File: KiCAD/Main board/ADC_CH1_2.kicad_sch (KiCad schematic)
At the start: 31 parts, among them U27 PCM1804, U5 OPA1632DR, U6 LM4562

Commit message: Worked on main board SCH
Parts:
- removed C21, C25, C26: 100nF, symbol Device:C
- removed C22, C28, C30, C4: 22uF, symbol Device:C_Polarized
- removed C35: 100n, symbol Device:C
- removed R31, R32, R36, R38: 10, symbol Device:R
- added C1 (x4): 100n, Capacitor_SMD:C_0402_1005Metric, symbol Device:C
- added C3 (x4): 22uF, Capacitor_THT:CP_Radial_D5.0mm_P2.00mm, symbol Device:C_Polarized
- added R1 (x4): 10R, Resistor_SMD:R_0805_2012Metric, symbol Device:R
- R13: value 2.7k -> 2k7
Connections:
- net +12V: now also R1.1, R1.1
- net -12V: now also R1.2, R1.2
- net GND: now also C1.1, C1.1, C1.2, C1.2, C3.1, C3.1, C3.2, C3.2
- net at U6.8 (V+): now also C1.1, C3.1, R1.2
- net at U5.3 (V+): now also C1.1, C3.1, R1.2
- net at U6.4 (V-): now also C1.2, C3.2, R1.1
- net at U5.6 (V-): now also C1.2, C3.2, R1.1
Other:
- moved on the sheet: C40, R45, U6B, U6C

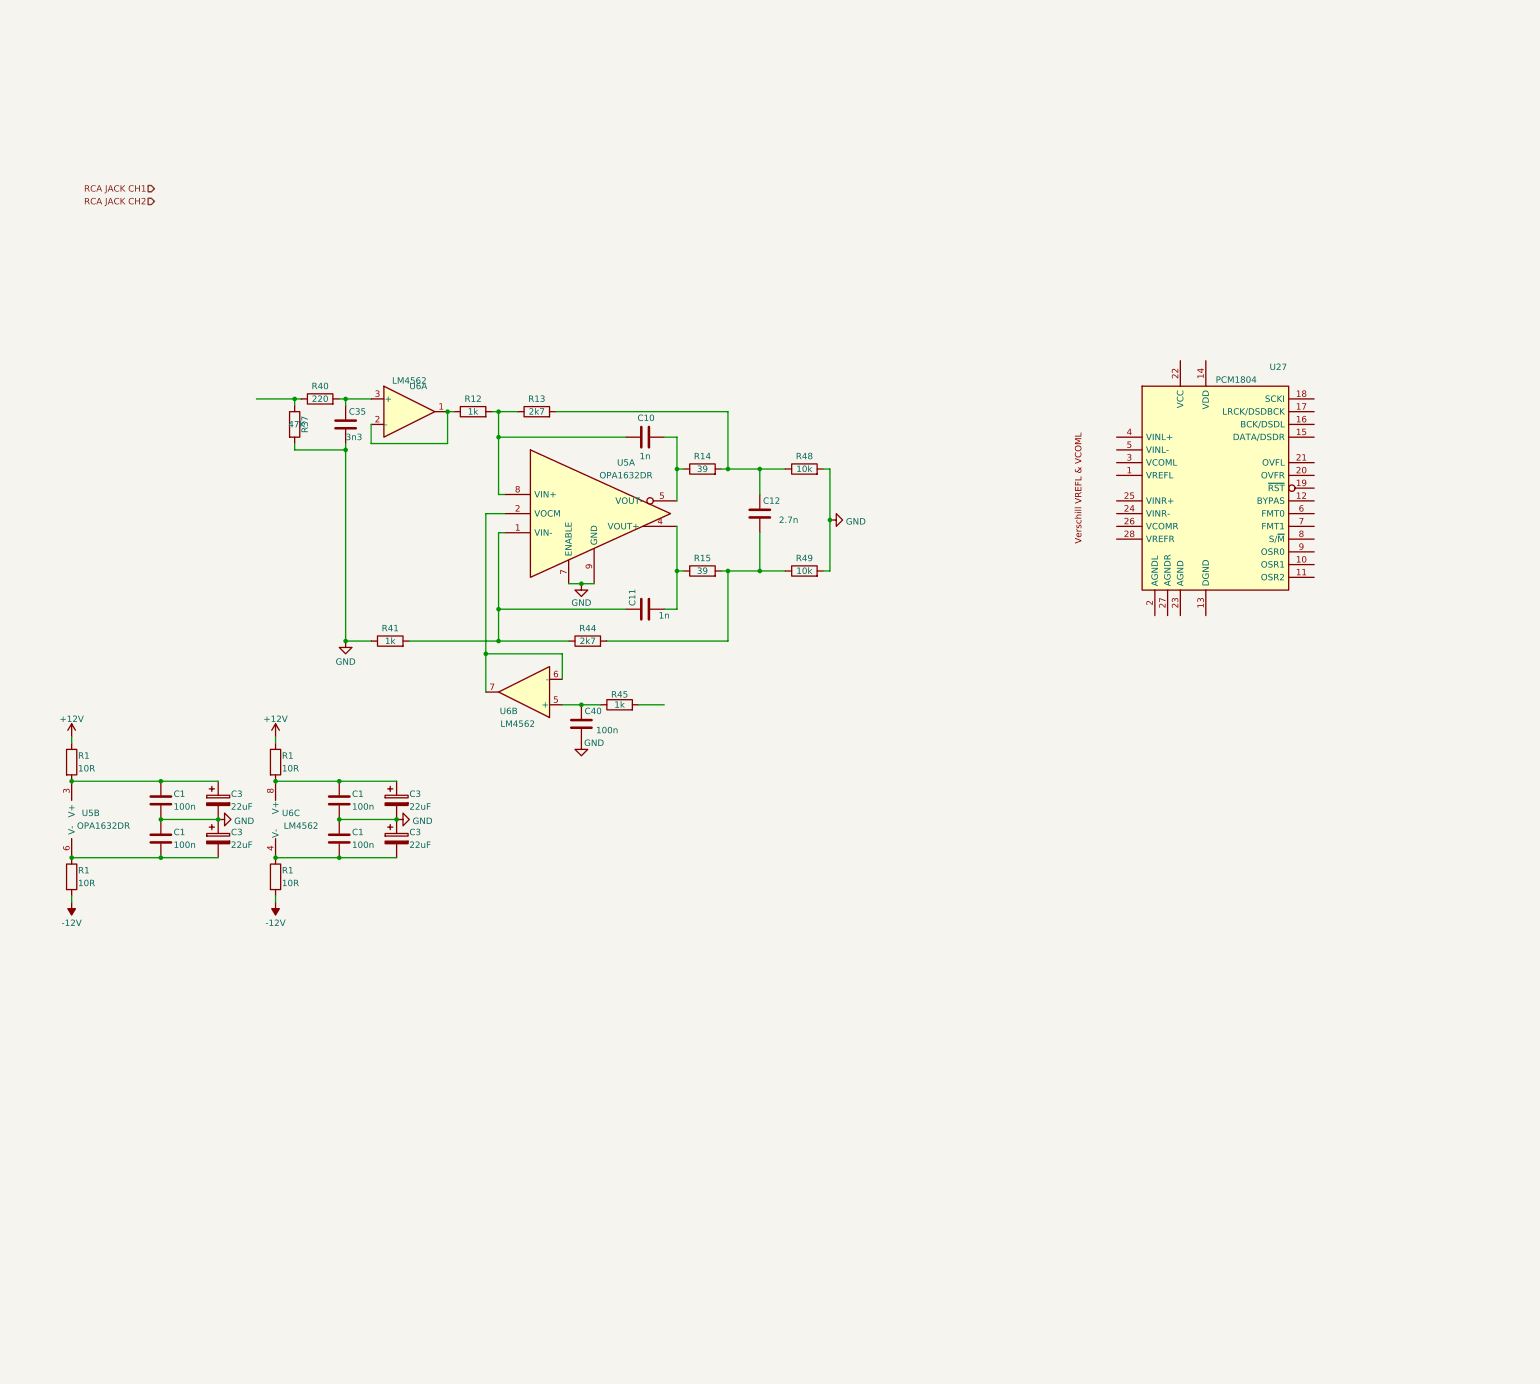
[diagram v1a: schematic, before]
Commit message: Worked on main board schematic and PCB, added symbols to symbol library
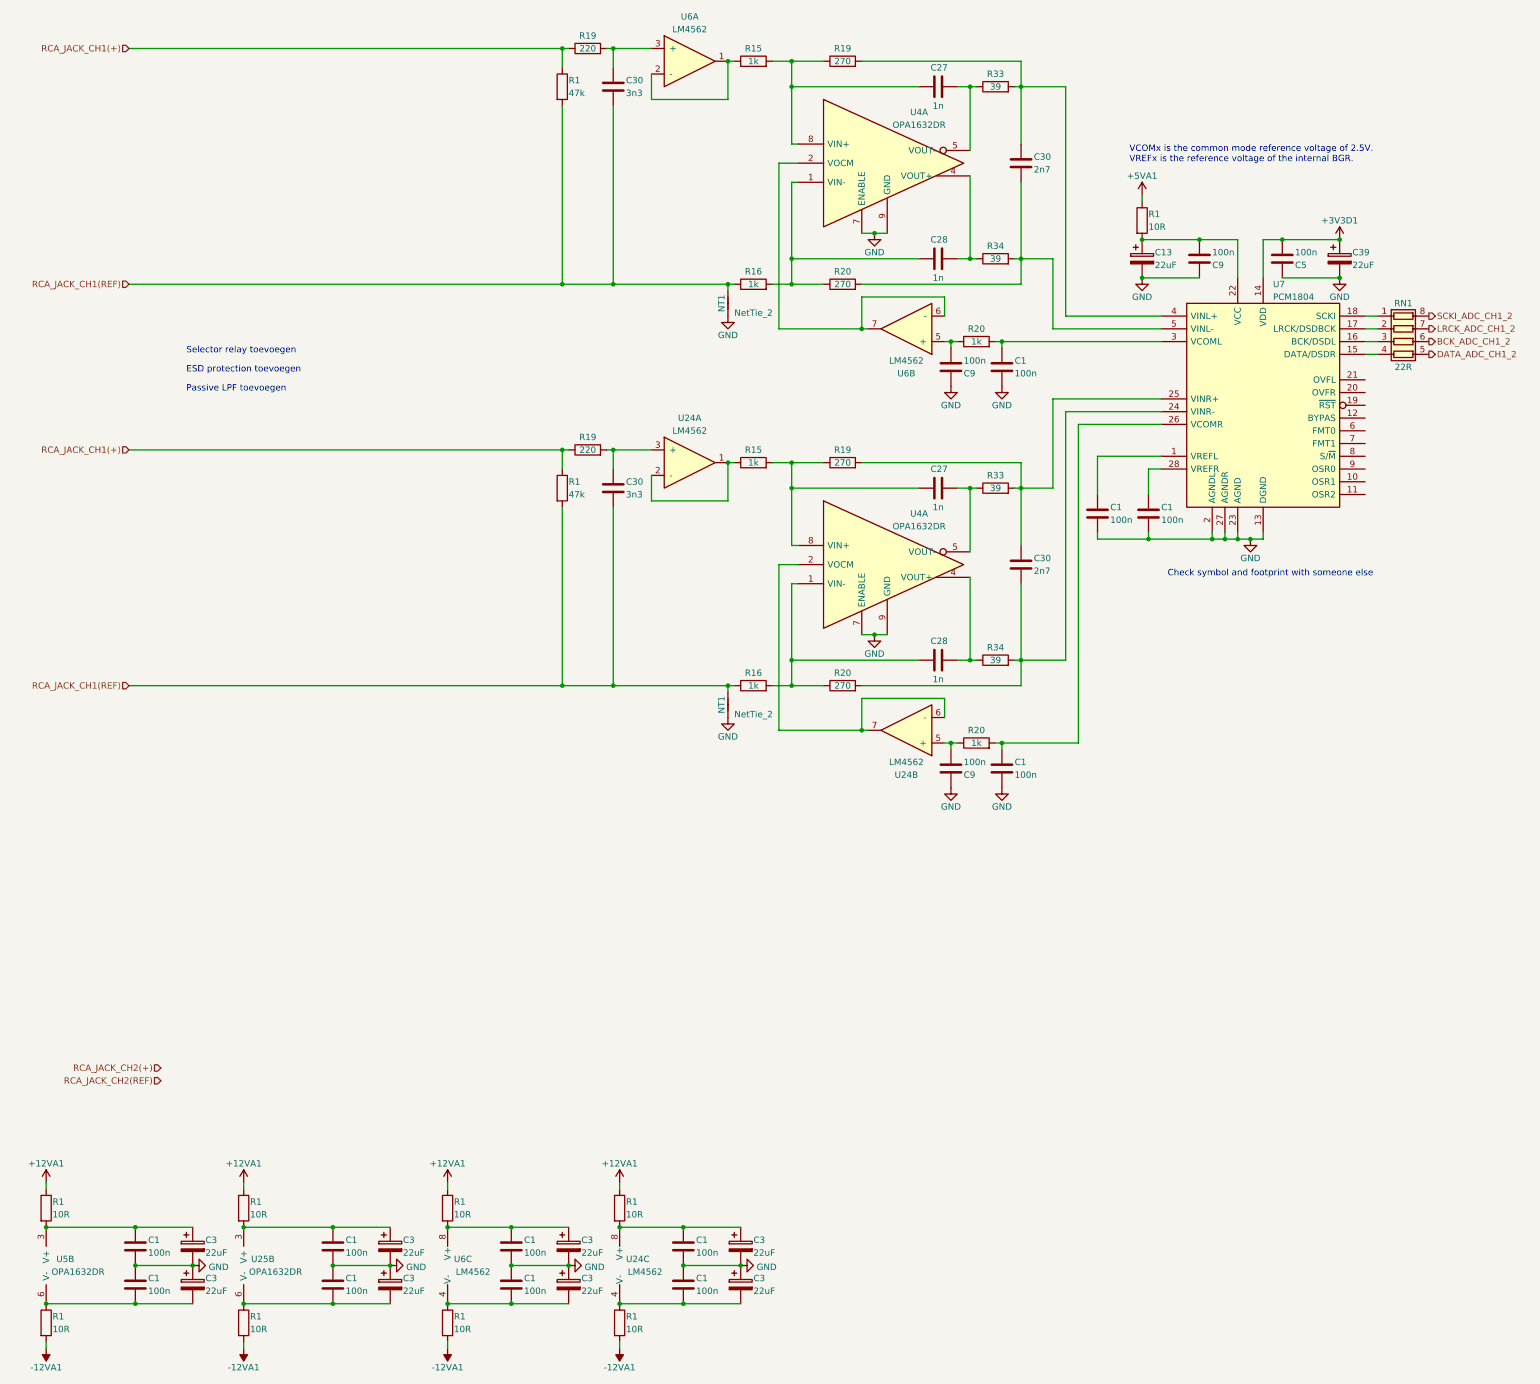
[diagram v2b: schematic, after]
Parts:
- removed C10, C11: 1n, symbol Device:C
- removed C12: 2.7n, symbol Device:C
- removed C35: 3n3, symbol Device:C
- removed C40: 100n, symbol Device:C
- removed R12, R41, R45: 1k, symbol Device:R
- removed R13, R44: 2k7, symbol Device:R
- removed R14, R15: 39, symbol Device:R
- removed R37: 47K, symbol Device:R
- removed R40: 220, symbol Device:R
- removed R48, R49: 10k, symbol Device:R
- removed U27: PCM1804, Package_SO:SSOP-28_5.3x10.2mm_P0.65mm, symbol Audio-DSP:PCM1804
- removed unit 1 of U5
- removed unit 2 of U6
- removed unit 1 of U6
- added C1 (x8), C5, C9 (x3): 100n, Capacitor_SMD:C_0402_1005Metric, symbol Device:C
- added C13, C3 (x4), C39: 22uF, Capacitor_THT:CP_Radial_D5.0mm_P2.00mm, symbol Device:C_Polarized
- added C27 (x2), C28 (x2): 1n, Capacitor_SMD:C_0805_2012Metric, symbol Device:C
- added C30 (x2): 2n7, Capacitor_SMD:C_0805_2012Metric, symbol Device:C
- added C30 (x2): 3n3, Capacitor_SMD:C_0805_2012Metric, symbol Device:C
- added NT1 (x2): NetTie_2, Audio-DSP:NetTie-2_SMD_Pad0.3mm, symbol Device:NetTie_2
- added R1 (x2): 47k, Resistor_SMD:R_0805_2012Metric, symbol Device:R
- added R1 (x5): 10R, Resistor_SMD:R_0805_2012Metric, symbol Device:R
- added R15 (x2), R16 (x2), R20 (x2): 1k, Resistor_SMD:R_0805_2012Metric, symbol Device:R
- added R19 (x2): 220, Resistor_SMD:R_0805_2012Metric, symbol Device:R
- added R19 (x2), R20 (x2): 270, Resistor_SMD:R_0805_2012Metric, symbol Device:R
- added R33 (x2), R34 (x2): 39, Resistor_SMD:R_0805_2012Metric, symbol Device:R
- added RN1: 22R, Resistor_SMD:R_Array_Convex_4x0402, symbol Device:R_Pack04
- added U24: LM4562, Package_SO:SOIC-8_3.9x4.9mm_P1.27mm, symbol Audio-DSP:LM4562
- added U25, U4 (x2): OPA1632DR, Audio-DSP:VSSOP-8_3.0x3.0mm_P0.65_TP1.8x1.5, symbol Audio-DSP:OPA1632DR
- added unit 1 of U6
- added unit 2 of U6
- added U7: PCM1804, Package_SO:SSOP-28_5.3x10.2mm_P0.65mm, symbol Audio_DSP:PCM1804
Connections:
- net GND: now also C1.1, C1.1, C1.2, C1.2, C1.2, C1.2, C1.2, C1.2, C13.2, C3.1, C3.1, C3.2, C3.2, C39.2, C5.1, C9.1, C9.1, C9.1, NT1.1, NT1.1, U4.7 (ENABLE), U4.7 (ENABLE), U4.9 (GND), U4.9 (GND), U7.13 (DGND), U7.2 (AGNDL), U7.23 (AGND), U7.27 (AGNDR)
- net +12V renamed +12VA1
- net +12VA1: now also R1.1, R1.1
- net -12V renamed -12VA1
- net -12VA1: now also R1.2, R1.2
- new net: C30.1, R19.2, R33.2, U7.4 (VINL+)
- new net: C30.2, R20.2, R34.2, U7.5 (VINL-)
- new net: R15.1, U6.1, U6.2 (-)
- new net: C27.1, R15.2, R19.1, U4.8 (VIN+) (x2)
- new net: C27.2, R33.1, U4.5 (VOUT-) (x2)
- new net: C30.1, R19.2, R33.2, U7.25 (VINR+)
- new net: C30.1, R19.2, U6.3 (+)
- new net: C28.1, R16.2, R20.1, U4.1 (VIN-) (x2)
- new net: C30.2, R20.2, R34.2, U7.24 (VINR-)
- new net: C1.1, C3.1, R1.2, U25.3 (V+)
- new net: C30.1, R19.2, U24.3 (+)
- new net: C9.2, R20.1, U24.5 (+)
- new net: C1.1, R20.2, U7.26 (VCOMR)
- new net: RN1.1 (R1.1), U7.18 (SCKI)
- new net: RN1.2 (R2.1), U7.17 (LRCK/DSDBCK)
- new net: RN1.3 (R3.1), U7.16 (BCK/DSDL)
- new net: RN1.4 (R4.1), U7.15 (DATA/DSDR)
- new net: C1.1, C3.1, R1.2, U24.8 (V+)
- new net: C1.2, C3.2, R1.1, U25.6 (V-)
- new net: C28.2, R34.1, U4.4 (VOUT+) (x2)
- new net: C13.1, C9.2, R1.2, U7.22 (VCC)
- new net: R15.1, U24.1, U24.2 (-)
- new net: C1.1, U7.1 (VREFL)
- new net: C9.2, R20.1, U6.5 (+)
- new net: U4.2 (VOCM), U6.6 (-), U6.7
- new net: C1.2, C3.2, R1.1, U24.4 (V-)
- new net: C1.1, R20.2, U7.3 (VCOML)
- new net: C1.1, U7.28 (VREFR)
- new net: U24.6 (-), U24.7, U4.2 (VOCM)
- new net +3V3D1: C39.1, C5.2, U7.14 (VDD)
- new net +5VA1: R1.1
- new net BCK_ADC_CH1_2: RN1.6 (R3.2)
- new net DATA_ADC_CH1_2: RN1.5 (R4.2)
- new net LRCK_ADC_CH1_2: RN1.7 (R2.2)
- new net RCA_JACK_CH1(+): R1.1, R1.1, R19.1, R19.1
- new net RCA_JACK_CH1(REF): C30.2, C30.2, NT1.2, NT1.2, R1.2, R1.2, R16.1, R16.1
- new net SCKI_ADC_CH1_2: RN1.8 (R1.2)
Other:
- note added: "Check symbol and footprint with someone else"
- note added: "ESD protection toevoegen"
- note added: "Passive LPF toevoegen"
- note added: "Selector relay toevoegen"
- note added: "VCOMx is the common mode reference voltage of 2.5V. VREFx is the reference voltage of the internal BGR."
- moved on the sheet: C1, C3, R1, U5B, U6C

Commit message: Worked on main board design
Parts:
- added C1 (x4): 100n, Capacitor_SMD:C_0402_1005Metric, symbol Device:C
- added D1, D2: 1N4148WS, Diode_SMD:D_SOD-323, symbol Diode:1N4148WS
- added D3: STS321050B100, Diode_SMD:D_SOD-323, symbol Device:D_TVS
- added D4: D_TVS, Diode_SMD:D_SOD-323, symbol Device:D_TVS
- added K1, K2: EA2-12NU, Audio-DSP:EA2-12NU, symbol Audio-DSP:EA2-12NU
- added Q1, Q2: BC847, Package_TO_SOT_SMD:SOT-23, symbol Transistor_BJT:BC847
- added R1 (x4): 10R, Resistor_SMD:R_0805_2012Metric, symbol Device:R
- added R20 (x2): 1k, Resistor_SMD:R_0805_2012Metric, symbol Device:R
- added R5 (x4): 1k, Resistor_SMD:R_0402_1005Metric, symbol Device:R
- added U34, U35: TL072, Package_SO:SOIC-8_3.9x4.9mm_P1.27mm, symbol Audio-DSP:TL072
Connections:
- net +12VA1: now also R1.1, R1.1, R5.2, R5.2
- net -12VA1: now also R1.2, R1.2
- net GND: now also Q1.2 (E), Q2.2 (E), R5.1, R5.1
- net at C30.1, R19.2, U6.3 (+): now also D3.2 (A2)
- net at C30.1, R19.2, U24.3 (+): now also D4.2 (A2)
- net RCA_JACK_CH1(+): no longer names the net of R1.1, R19.1
- net RCA_JACK_CH1(+): now also K2.3; no longer R1.1, R19.1
- net RCA_JACK_CH1(REF): no longer names the net of C30.2, NT1.2, R1.2, R16.1
- net RCA_JACK_CH1(REF): now also D3.1 (A1), K1.8; no longer C30.2, NT1.2, R1.2, R16.1
- new net: D1.2 (A), K1.10, Q1.3 (C)
- new net: C1.1, C1.2 (x2)
- new net: C1.2, R1.1, U34.4 (V-)
- new net: K1.3, R1.1, R19.1
- new net: C30.2, D4.1 (A1), K2.8, NT1.2, R1.2, R16.1
- new net: C1.1, R1.2, U35.8 (V+)
- new net: R5.1, U35.6 (-)
- new net: C1.2, R1.1, U35.4 (V-)
- new net: R5.2, U35.5 (+)
- new net: C1.1, R1.2, U34.8 (V+)
- new net: R5.2, U34.5 (+)
- new net: Q2.1 (B), R20.1
- new net: D2.2 (A), K2.10, Q2.3 (C)
- new net: R5.1, U34.6 (-)
- new net: U35.1, U35.2 (-)
- new net: U34.1, U34.2 (-)
- new net: Q1.1 (B), R20.1
- new net +12VD1: D1.1 (K), D2.1 (K), K1.1, K2.1
- new net INPUT_SELECTOR_RELAY_CH1: R20.2
- new net INPUT_SELECTOR_RELAY_CH2: R20.2
- new net JACK_CH1(+): K1.4
- new net JACK_CH1(REF): K1.7
- new net JACK_CH2(+): K2.4
- new net JACK_CH2(REF): K2.7
- new net RCA_CH1(+): K1.2
- new net RCA_CH1(REF): K1.9
- new net RCA_CH2(+): K2.2
- new net RCA_CH2(REF): K2.9
- no-connect marks 0 -> 2
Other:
- note added: "DC-offset creëren voor comparator?"
- note added: "INPUT_SELECTOR_RELAY LOW=RCA HIGH-Jack"
- note removed: "ESD protection toevoegen"
- note removed: "Passive LPF toevoegen"
- note removed: "Selector relay toevoegen"
- moved on the sheet: C1, C13, C27, C28, C30, C39, C5, C9, NT1, R1, R15, R16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

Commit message: Worked on main board
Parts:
- added U36 (x2): LM339, symbol Comparator:LM339
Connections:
- new net VU_LED1_CH1: U36.2
- new net VU_LED1_CH2: U36.2
- new net VU_LED2_CH1: U36.1
- new net VU_LED2_CH2: U36.1
- new net VU_LED3_CH1: U36.13
- new net VU_LED3_CH2: U36.13
- new net VU_LED4_CH1: U36.14
- new net VU_LED4_CH2: U36.14

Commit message: Worked on main board
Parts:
- added U38: PGA2311P, Package_DIP:DIP-16_W7.62mm, symbol Audio_DSP:PGA2311P
- U36: footprint (none) -> Package_SO:TSSOP-14_4.4x5mm_P0.65mm
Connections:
- net GND: now also U36.12 (V-), U36.12 (V-)
- net at C30.1, D3.2 (A2), R19.2: no longer U6.3 (+)
- net at C30.1, D4.2 (A2), R19.2: no longer U24.3 (+)
- net at C30.2, D3.1 (A1), K1.8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: no longer NT1.2, R16.1
- net +5VD1: now reaches U36.3 (V+)
- net +5VD1: now also U36.3 (V+)
- net at C30.2, D4.1 (A1), K2.8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: no longer NT1.2, R16.1
- new net: NT1.2, R16.1 (x2)
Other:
- note added: "CS aan GND hangen"
- note added: "MUTE pull-up?"
- note added: "SDO kruisje"

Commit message: Worked in main board
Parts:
- added C13 (x2), C39: 22uF, Capacitor_THT:CP_Radial_D5.0mm_P2.00mm, symbol Device:C_Polarized
- added C5 (x3), C9 (x2): 100n, Capacitor_SMD:C_0402_1005Metric, symbol Device:C
- added NT1 (x2): NetTie_2, Audio-DSP:NetTie-2_SMD_Pad0.3mm, symbol Device:NetTie_2
- added Q3: BC847, Package_TO_SOT_SMD:SOT-23, symbol Transistor_BJT:BC847
- added R1 (x2): 10R, Resistor_SMD:R_0805_2012Metric, symbol Device:R
- added R1 (x2): 10k, Resistor_SMD:R_0805_2012Metric, symbol Device:R
- added R20: 1k, Resistor_SMD:R_0805_2012Metric, symbol Device:R
- added U39: TXS0102, Package_SO:VSSOP-8_2.4x2.1mm_P0.5mm, symbol Audio-DSP:TXS0102
- D4: value D_TVS -> STS321050B100
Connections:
- net +3V3D1: now also U7.10 (OSR1), U7.11 (OSR2), U7.6 (FMT0), U7.9 (OSR0), C5.2, U39.3 (VCCA)
- net +5VA1: now also R1.1
- net +5VD1: now also U38.1 (ZCEN), U38.4 (VD+), U38.8 (~{MUTE}), C39.1, C5.2, C5.2, R1.1, R1.1, U39.2 (VCCB)
- net GND: now also U38.2 (~{CS}), U38.5 (DGND), U7.12 (BYPAS), U7.7 (FMT1), U7.8 (S/~{M}), C13.1, C13.2, C39.2, C5.1, C5.1, C5.1, C9.1, C9.1, NT1.1, NT1.1, Q3.2 (E), U39.2 (VCCB)
- net at U6.3 (+): now also U38.14 (VOUTL)
- net at C30.1, D4.2 (A2), R19.2: now also U35.3 (+), U38.9 (VINR)
- net at C30.2, D3.1 (A1), K1.8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: now also U38.15 (AGNDL), NT1.2
- net at C30.2, D4.1 (A1), K2.8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: now also U38.10 (AGNDR), NT1.2
- net at C30.1, D3.2 (A2), R19.2: now also U34.3 (+), U38.16 (VINL)
- net at U24.3 (+): now also U38.11 (VOUTR)
- net ~{RST_ADC_CH1_2}: now reaches U7.19 (~{RST})
- net at U38.12 (VA+): now also C13.1, C9.2, R1.2
- net at U38.13 (VA-): now also C13.2, C9.2, R1.2
- net at U38.3 (SDI): now also U39.1 (B2)
- net at U38.6 (SCLK): now also U39.8 (B1)
- new net: Q3.1 (B), R1.2, R20.1
- new net: Q3.3 (C), R1.2, U39.6 (OE)
- new net -5VA1: R1.1
- new net TXS0102_SCLK_CH1_2: U39.5 (A1)
- new net TXS0102_SDA_CH1_2: U39.4 (A2)
- new net ~{TXS0102_OE_CH1_2}: R20.2
- no-connect marks 2 -> 5
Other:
- note added: "Bidirectional level translator"
- note added: "C:\Users\PC\OneDrive\Documenten\School\Fontys\Minor\Be creative minor\Git\Audio-DSP\LTspice\Front-end"
- note added: "Check output impedance of PGA2311 Misschien kan deze buffer weg"
- note added: "HPF active"
- note added: "High side switch maken?"
- note added: "I2S format"
- note added: "Master mode"
- note added: "Precision rectifier"
- note added: "QUAD mode"
- note added: "RST kan ook aan +3V3D1"
- note added: "Unmuted"
- note added: "Zero crossing enabled"
- note removed: "CS aan GND hangen"
- note removed: "MUTE pull-up?"
- note removed: "SDO kruisje"
- moved on the sheet: C30, D3, K1B, K1C, K2B, K2C, R1, R19, U34A, U35A, U38

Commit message: Main board
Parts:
- removed R1 (x4): 10R, Resistor_SMD:R_0805_2012Metric, symbol Device:R
- removed R1 (x2): 10k, Resistor_SMD:R_0805_2012Metric, symbol Device:R
- removed R5 (x4): 1k, Resistor_SMD:R_0402_1005Metric, symbol Device:R
- added C1 (x4): 100n, Capacitor_SMD:C_0402_1005Metric, symbol Device:C
- added Q4: BC857, Package_TO_SOT_SMD:SOT-23, symbol Transistor_BJT:BC857
- added R1 (x2), R20: 10k, Resistor_SMD:R_0805_2012Metric, symbol Device:R
- added R20: 100k, Resistor_SMD:R_0805_2012Metric, symbol Device:R
- R20: value 1k -> 10k
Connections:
- net +5VD1: now also Q4.2 (E), R1.2; no longer U36.3 (V+), U36.3 (V+)
- net GND: now also C1.2, C1.2, R1.1
- net -15VD1: now reaches C1.2, U34.4 (V-)
- net -15VD1: now also C1.2, U35.4 (V-)
- net +15VD1: now reaches C1.1, U35.8 (V+)
- net +15VD1: now also C1.1, U34.8 (V+)
- net at U39.6 (OE): now also Q4.3 (C), R1.2; no longer Q3.3 (C)
- new net: Q4.1 (B), R1.1, R20.1
- new net: C1.1, U36.3 (V+) (x2)
- new net: C1.1, C1.2 (x2)
- new net: Q3.3 (C), R20.2
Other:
- note added: "+12V or +5V? ADC en VU-meter position"
- note removed: "C:\Users\PC\OneDrive\Documenten\School\Fontys\Minor\Be creative minor\Git\Audio-DSP\LTspice\Front-end"
- note removed: "High side switch maken?"
- moved on the sheet: Q3, R20, U36A, U36B, U36C, U36D, U36E
